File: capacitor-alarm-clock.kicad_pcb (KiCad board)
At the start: 2 copper layers, 105 x 67.5 mm, 79 parts

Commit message: Pretty much finished the PCB, only got the silkscreen decorations left
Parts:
- added D10: LED, LED_SMD:LED_0603_1608Metric, F.Cu at (29.0, 50.0)
- added D11: LED, LED_SMD:LED_0603_1608Metric, F.Cu at (44.5, 50.0)
- added D12: LED, LED_SMD:LED_0603_1608Metric, F.Cu at (60.0, 50.0)
- added R30: 1K, Resistor_SMD:R_0603_1608Metric, F.Cu at (31.0, 52.0)
- added R31: 1K, Resistor_SMD:R_0603_1608Metric, F.Cu at (46.5, 52.0)
- added R32: 1K, Resistor_SMD:R_0603_1608Metric, F.Cu at (62.0, 52.0)
- added REF**: MountingHole_2.2mm_M2, MountingHole:MountingHole_2.2mm_M2, F.Cu at (67.8, 84.5)
- added REF**: MountingHole_2.2mm_M2, MountingHole:MountingHole_2.2mm_M2, F.Cu at (32.8, 84.5)
- added REF**: MountingHole_2.2mm_M2, MountingHole:MountingHole_2.2mm_M2, F.Cu at (47.5, 38.5)
- moved C10 110.7 mm to (74.7, 61.0), turned to 90 degrees
- moved C9 107.5 mm to (74.7, 57.7), turned to 90 degrees
- moved U4 104.4 mm to (77.2, 67.8), turned to -90 degrees
- moved R22 94.3 mm to (72.2, 66.7)
- moved R21 90.3 mm to (72.7, 73.5), turned to -90 degrees
- moved D9 90.0 mm to (72.9, 64.5)
- moved R19 85.4 mm to (70.9, 69.7), turned to -90 degrees
- moved C12 84.1 mm to (72.7, 77.2), turned to 90 degrees
- moved R20 83.8 mm to (69.4, 69.7), turned to -90 degrees
- moved C11 83.3 mm to (74.7, 76.4), turned to 90 degrees
- moved C13 76.4 mm to (74.7, 67.5), turned to -90 degrees
- moved JTAG 58.6 mm to (68.0, 49.5)
- moved C15 56.4 mm to (74.7, 48.7), turned to 90 degrees
- moved R24 52.0 mm to (67.0, 53.0), turned to 90 degrees
- moved SW2 49.5 mm to (78.7, 51.7), turned to 90 degrees
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- renumbered H1 to 3V3, SW3 to BOOT, H5 to JTAG, SW1 to RESET, H3 to UART, H2 to VDC
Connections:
- net /ESP32/IO0 renamed /VDC_SENSE
- R23 pad 1: /ESP32/TMS -> /ESP32/SDA
- R23 pad 2: /ESP32/SDA -> /ESP32/TMS
- R24 pad 1: /ESP32/TDI -> /ESP32/SCK
- R24 pad 2: /ESP32/SCK -> /ESP32/TDI
- R25 pad 1: /ESP32/TCK -> /SW_R
- R25 pad 2: /SW_R -> /ESP32/TCK
- R26 pad 1: /ESP32/TDO -> /SW_L
- R26 pad 2: /SW_L -> /ESP32/TDO
- R7 pad 1: VDC -> VCC
- U1 pad 18: /ESP32/SDA -> /ESP32/TMS
- U1 pad 19: /ESP32/SCK -> /ESP32/TDI
- U1 pad 20: /SW_R -> /ESP32/TCK
- U1 pad 21: /SW_L -> /ESP32/TDO
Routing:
- net GND: track 0.00 -> 161.4 mm, vias 0 -> 37
- net VCC: track 0.00 -> 95.3 mm, vias 0 -> 1
- net +3V3: track 0.00 -> 68.6 mm, vias 0 -> 3
- net Vdrive: track 0.00 -> 63.1 mm
- net /VDC_SENSE: track 0.00 -> 48.5 mm, vias 0 -> 2
- net /USB/USB_D+: track 0.00 -> 47.6 mm, vias 0 -> 2
- net /USB/USB_D-: track 0.00 -> 47.5 mm, vias 0 -> 2
- net /ESP32/IO3: track 0.00 -> 46.3 mm, vias 0 -> 2
- net /SW_L: track 0.00 -> 36.8 mm, vias 0 -> 2
- net VBUS: track 0.00 -> 31.9 mm
- net /ESP32/IO1: track 0.00 -> 30.8 mm
- net /ESP32/SDA: track 0.00 -> 28.8 mm
- net /ESP32/SCK: track 0.00 -> 25.9 mm
- net /ESP32/EN: track 0.00 -> 22.8 mm, vias 0 -> 2
- net /ESP32/IO10: track 0.00 -> 20.8 mm
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- added copper zone on F.Cu, net +3V3
- added copper zone on B.Cu, net GND
- added copper zone on F.Cu, net GND
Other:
- board size 105 x 67.5 mm -> 62.3 x 64.3 mm
- board text added: "+"
- board text added: "-"
- board text added: "RX"
- board text added: "TX"

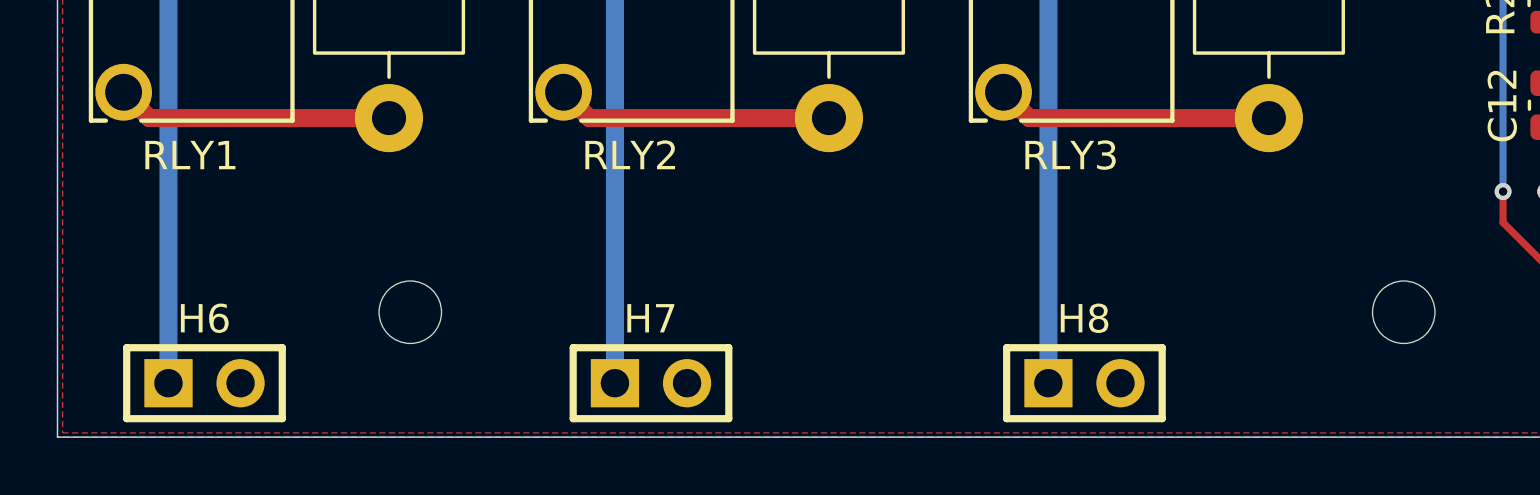
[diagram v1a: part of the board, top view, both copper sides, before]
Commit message: Update PCB silkscreen
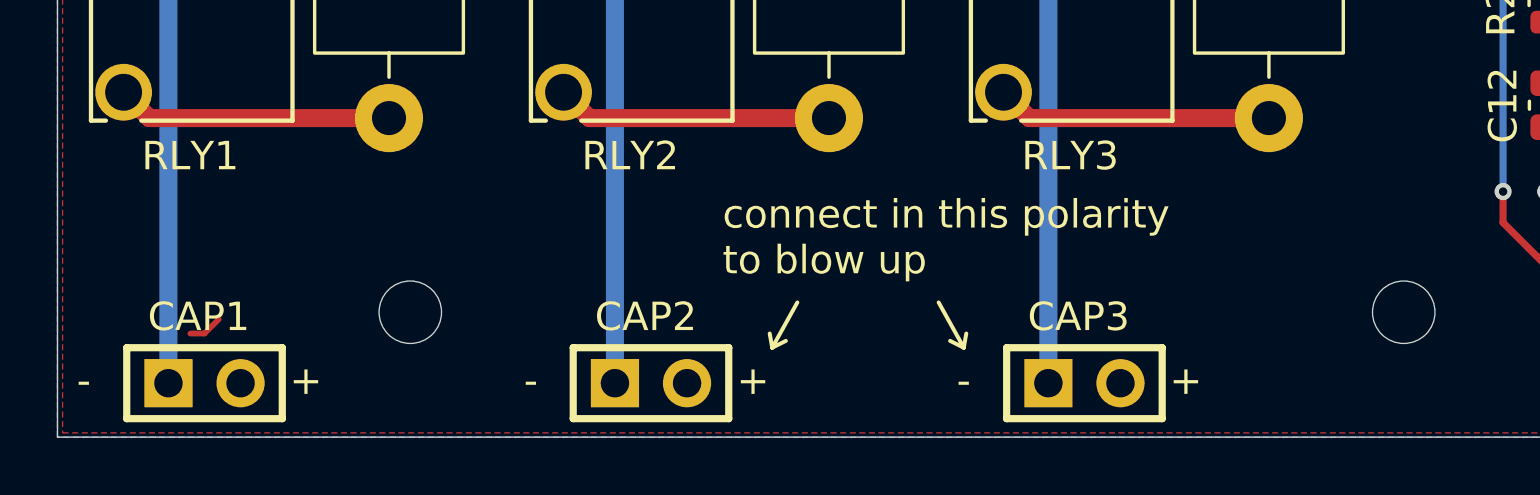
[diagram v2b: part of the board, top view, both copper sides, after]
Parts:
- added G***: LOGO, LOGO, B.Cu at (55.5, 50.8)
- added G*** (x2): LOGO, LOGO, B.Cu at (65.1, 34.4)
- added G*** (x2): LOGO, LOGO, B.Cu at (63.8, 69.5)
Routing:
- net (no net): track 0.00 -> 1.21 mm
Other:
- board text added: "CAP1"
- board text added: "CAP2"
- board text added: "CAP3"
- board text added: "capacitor alarm clock"
- board text added: "connect in this polarity to blow up"
- board text added: "github.com/arcaege/capacitor-alarm-clock"
- board text added: "honourable mentions: - tobycm - Rudy - KaiPereira - Cyao - shinkensen - 555 timer - tecknet"

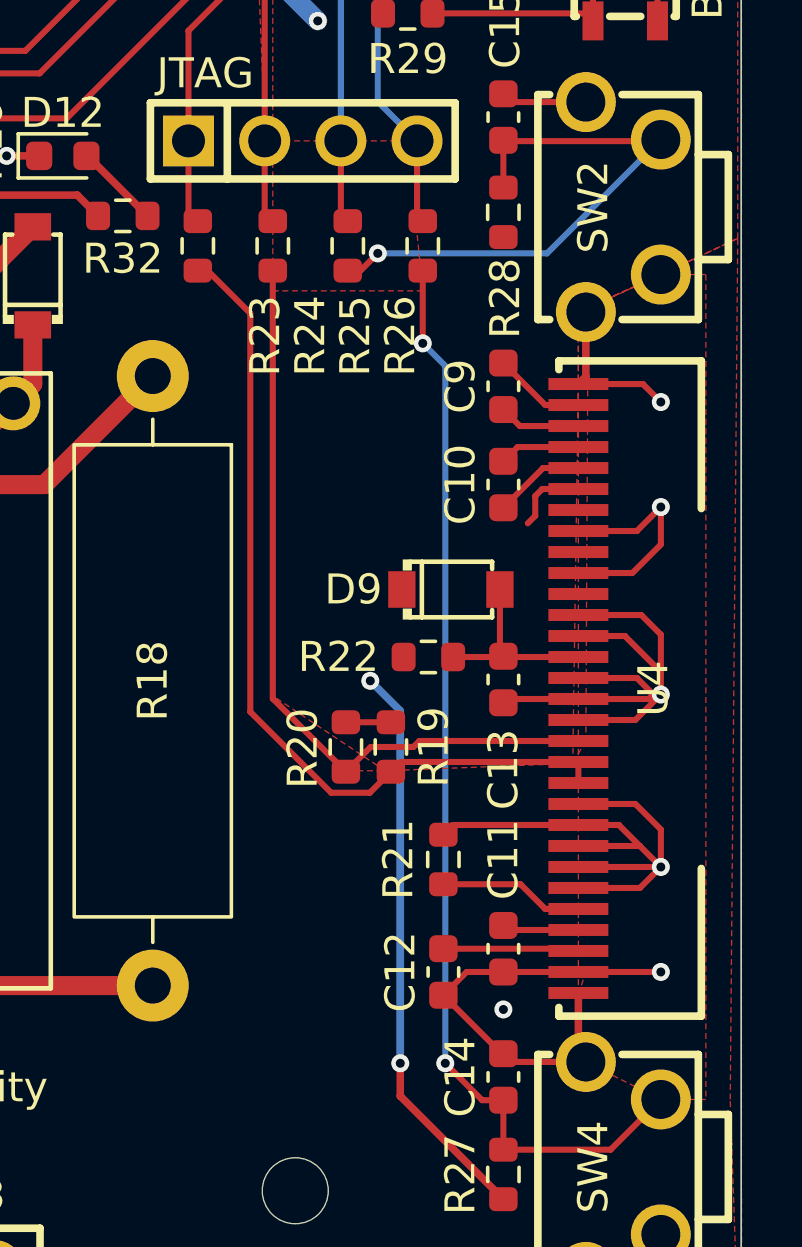
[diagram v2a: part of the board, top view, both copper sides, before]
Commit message: Flipped the display footprint so it faces the correct way
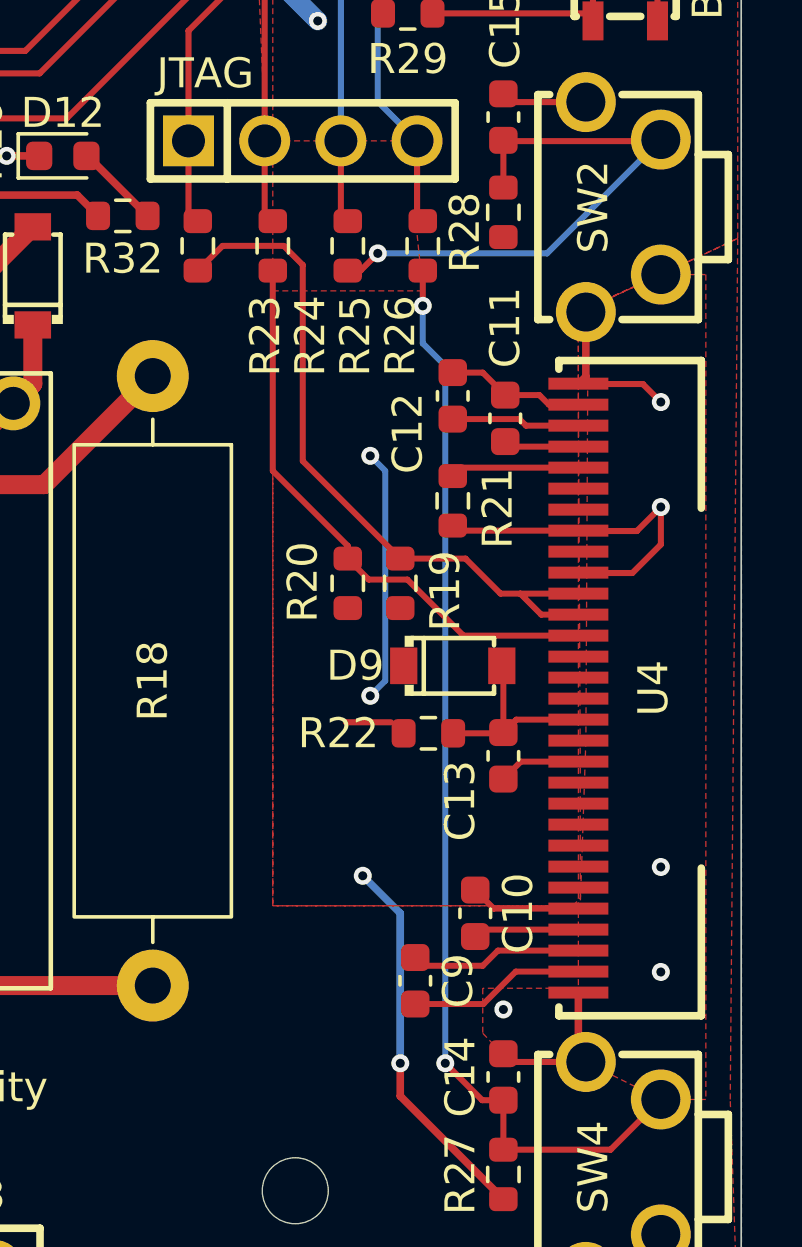
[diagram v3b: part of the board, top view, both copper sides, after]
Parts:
- moved C9 20.0 mm to (71.8, 77.5), turned to -90 degrees
- moved C12 19.2 mm to (73.0, 58.0), turned to -90 degrees
- moved C11 17.7 mm to (74.8, 58.8), turned to -90 degrees
- moved C10 14.3 mm to (73.8, 75.2), turned to -90 degrees
- moved R21 12.0 mm to (73.0, 61.5), turned to 90 degrees
- moved R19 5.47 mm to (71.2, 64.2), turned to 90 degrees
- moved R20 5.46 mm to (69.5, 64.2), turned to 90 degrees
- moved D9 2.54 mm to (73.0, 67.0)
- moved C13 2.54 mm to (74.7, 70.0)
- moved R22 2.54 mm to (72.2, 69.2)
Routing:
- net GND: track 161.4 -> 122.9 mm, vias 37 -> 36
- net /ESP32/SCK: track 25.9 -> 19.4 mm
- net /ESP32/SDA: track 28.8 -> 23.9 mm
- net Net-(U4-C2N): track 2.73 -> 5.76 mm
- net Net-(U4-C2P): track 3.08 -> 5.89 mm
- net Net-(U4-C1P): track 2.70 -> 3.53 mm
- net Net-(U4-C1N): track 3.05 -> 3.69 mm
- net Net-(U4-IREF): track 4.84 -> 4.30 mm
- net +3V3: track 68.6 -> 68.1 mm, vias 3 -> 5
